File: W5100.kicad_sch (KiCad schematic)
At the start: 71 parts, among them J1 ARJM11C7-114-BA-EW2, T1 FA2805, U2 W5100, U3 TLV431DBZ, U4 VO615A, U5 SI3402, Y2 25MHz

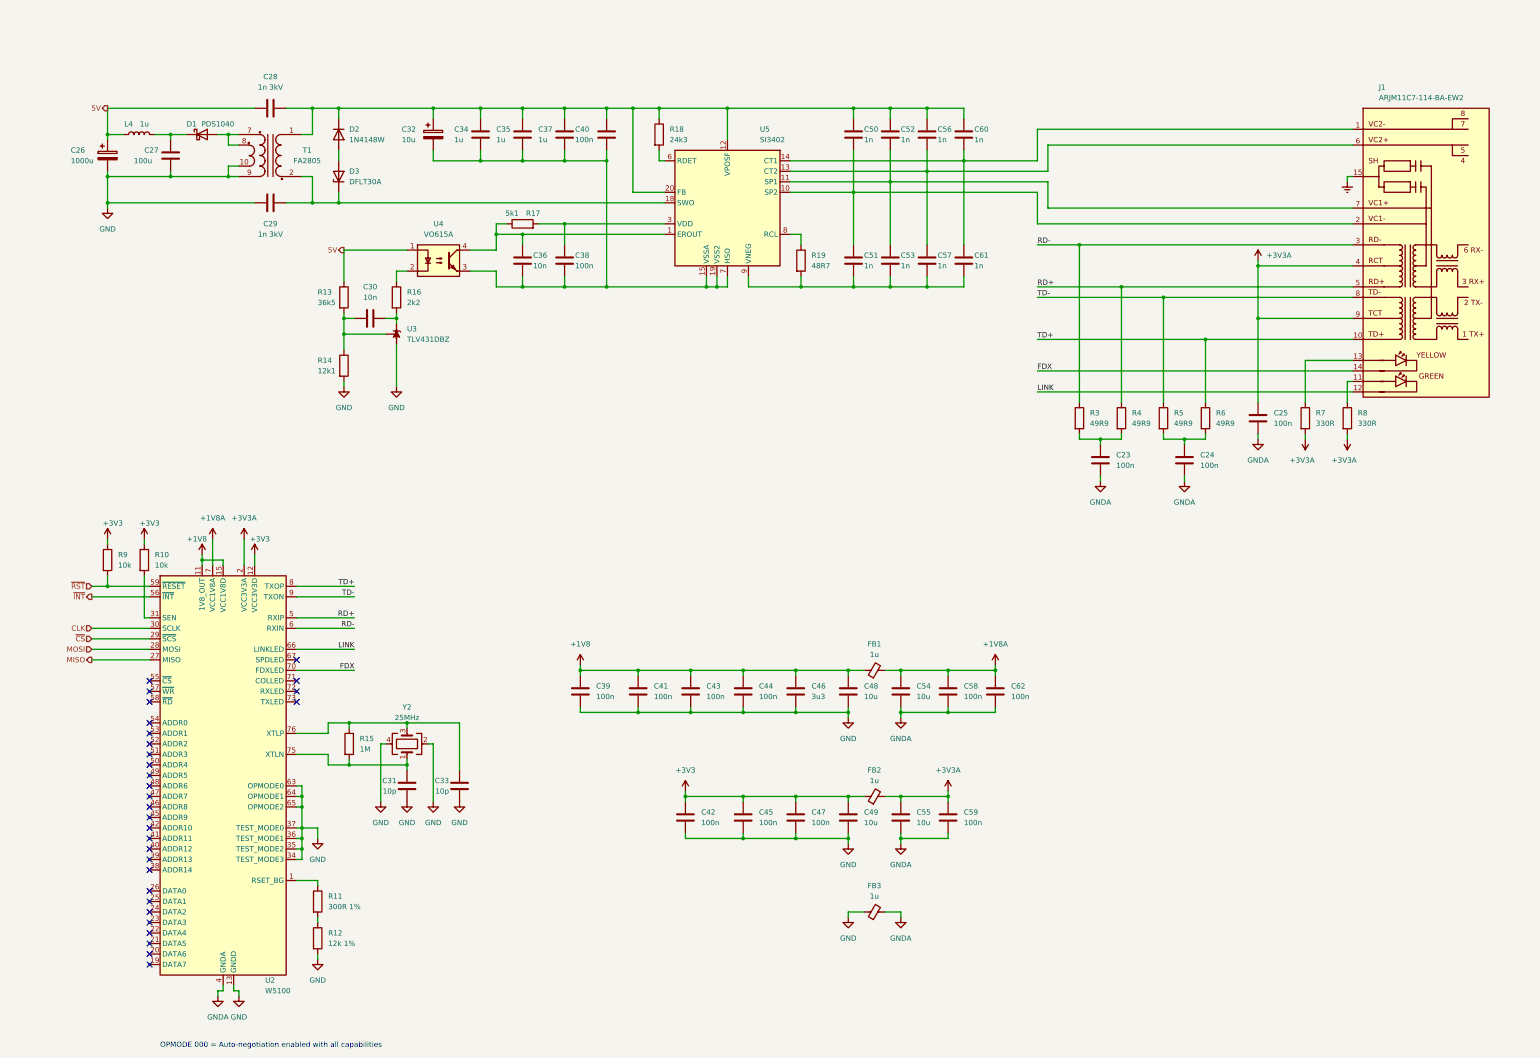
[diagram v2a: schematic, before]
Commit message: Added USB port
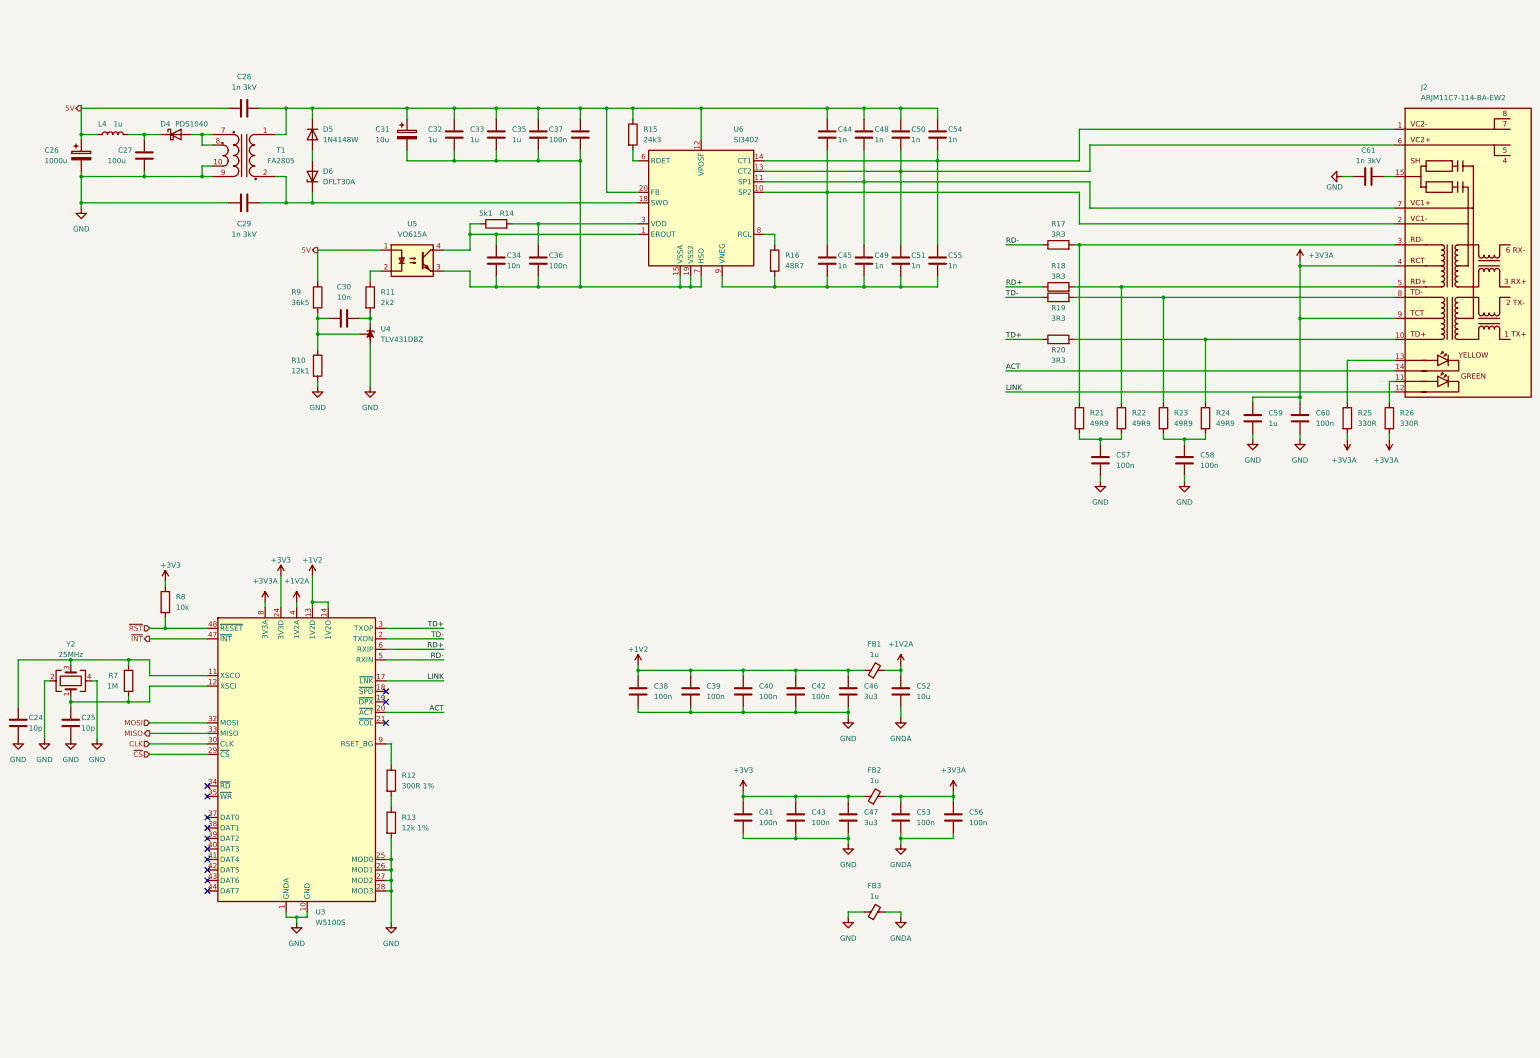
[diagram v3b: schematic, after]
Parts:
- removed C31, C33: 10p, symbol Device:C
- removed C42, C58, C62: 100n, symbol Device:C
- removed C48, C55: 10u, symbol Device:C
- removed R10, R9: 10k, symbol Device:R
- removed R11: 300R 1%, symbol Device:R
- removed R15: 1M, symbol Device:R
- removed U2: W5100, Package_QFP:LQFP-80_10x10mm_P0.4mm, symbol Interface_Ethernet:W5100
- added C24, C25: 10p, Capacitor_SMD:C_0402_1005Metric, symbol Device:C
- added C56: 100n, Capacitor_SMD:C_0402_1005Metric, symbol Device:C
- added C59: 1u, Capacitor_SMD:C_0402_1005Metric, symbol Device:C
- added C61: 1n 3kV, symbol Device:C
- added R13: 12k 1%, Resistor_SMD:R_0402_1005Metric, symbol Device:R
- added R17, R18, R19, R20: 3R3, Resistor_SMD:R_0402_1005Metric, symbol Device:R
- added R7: 1M, Resistor_SMD:R_0402_1005Metric, symbol Device:R
- added R8: 10k, Resistor_SMD:R_0402_1005Metric, symbol Device:R
- added U3: W5100S, Package_DFN_QFN:QFN-48-1EP_7x7mm_P0.5mm_EP5.3x5.3mm, symbol wiznet:W5100S
- C30, FB1, FB2, FB3, L4: footprint (none) -> Capacitor_SMD:C_0402_1005Metric
- C31: renamed from C32; footprint (none) -> Capacitor_SMD:C_0402_1005Metric
- C32: renamed from C34; footprint (none) -> Capacitor_SMD:C_0402_1005Metric
- C33: renamed from C35; footprint (none) -> Capacitor_SMD:C_0402_1005Metric
- C34: renamed from C36; footprint (none) -> Capacitor_SMD:C_0402_1005Metric
- C35: renamed from C37; footprint (none) -> Capacitor_SMD:C_0402_1005Metric
- C36: renamed from C38; footprint (none) -> Capacitor_SMD:C_0402_1005Metric
- C37: renamed from C40; footprint (none) -> Capacitor_SMD:C_0402_1005Metric
- C38: renamed from C39; footprint (none) -> Capacitor_SMD:C_0402_1005Metric
- C39: renamed from C41; footprint (none) -> Capacitor_SMD:C_0402_1005Metric
- C40: renamed from C43; footprint (none) -> Capacitor_SMD:C_0402_1005Metric
- C41: renamed from C45; footprint (none) -> Capacitor_SMD:C_0402_1005Metric
- C42: renamed from C44; footprint (none) -> Capacitor_SMD:C_0402_1005Metric
- C43: renamed from C47; footprint (none) -> Capacitor_SMD:C_0402_1005Metric
- C44: renamed from C50; footprint (none) -> Capacitor_SMD:C_0402_1005Metric
- C45: renamed from C51; footprint (none) -> Capacitor_SMD:C_0402_1005Metric
- C47: renamed from C49; value 10u -> 3u3
- C48: renamed from C52; footprint (none) -> Capacitor_SMD:C_0402_1005Metric
- C49: renamed from C53; footprint (none) -> Capacitor_SMD:C_0402_1005Metric
- C50: renamed from C56; footprint (none) -> Capacitor_SMD:C_0402_1005Metric
- C51: renamed from C57; footprint (none) -> Capacitor_SMD:C_0402_1005Metric
- C53: renamed from C59; footprint (none) -> Capacitor_SMD:C_0402_1005Metric
- C54: renamed from C60; footprint (none) -> Capacitor_SMD:C_0402_1005Metric
- C55: renamed from C61; footprint (none) -> Capacitor_SMD:C_0402_1005Metric
- C57: renamed from C23; footprint (none) -> Capacitor_SMD:C_0402_1005Metric
- C58: renamed from C24; footprint (none) -> Capacitor_SMD:C_0402_1005Metric
- C60: renamed from C25; footprint (none) -> Capacitor_SMD:C_0402_1005Metric
- R10: renamed from R14; footprint (none) -> Resistor_SMD:R_0402_1005Metric
- R11: renamed from R16; footprint (none) -> Resistor_SMD:R_0402_1005Metric
- R12: value 12k 1% -> 300R 1%; footprint (none) -> Resistor_SMD:R_0402_1005Metric
- R14: renamed from R17; footprint (none) -> Resistor_SMD:R_0402_1005Metric
- R15: renamed from R18; footprint (none) -> Resistor_SMD:R_0402_1005Metric
- R16: renamed from R19; footprint (none) -> Resistor_SMD:R_0402_1005Metric
- R21: renamed from R3; footprint (none) -> Resistor_SMD:R_0402_1005Metric
- R22: renamed from R4; footprint (none) -> Resistor_SMD:R_0402_1005Metric
- R23: renamed from R5; footprint (none) -> Resistor_SMD:R_0402_1005Metric
- R24: renamed from R6; footprint (none) -> Resistor_SMD:R_0402_1005Metric
- R25: renamed from R7; footprint (none) -> Resistor_SMD:R_0402_1005Metric
- R26: renamed from R8; footprint (none) -> Resistor_SMD:R_0402_1005Metric
- R9: renamed from R13; footprint (none) -> Resistor_SMD:R_0402_1005Metric
- T1: footprint (none) -> coilcraft:Transformer_Coilcraft_Si3402
- U6: renamed from U5; footprint (none) -> skyworks:Skyworks_QFN-20_1EP5x5mm_P0.8mm_EP2.7x2.7mm
- renumbered C54 to C52, D1 to D4, D2 to D5, D3 to D6, J1 to J2, U3 to U4, U4 to U5
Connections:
- net +3V3: now also R8.1, U3.24 (3V3D), U3.36 (3V3D)
- net +3V3A: now also C56.1, C59.1, U3.15 (3V3A), U3.8 (3V3A)
- net CLK: now also U3.30 (CLK)
- net GND: now also C57.2, C58.2, C60.2, C24.2, C25.2, C59.2, C61.1, R13.2, U3.1 (GNDA), U3.10 (GND), U3.16 (GNDA), U3.23 (GND), U3.25 (MOD0), U3.26 (MOD1), U3.27 (MOD2), U3.28 (MOD3), U3.46 (GND), U3.7 (GNDA); no longer R12.2
- net GNDA: now also C56.2; no longer C57.2, C58.2, C60.2
- net LINK: now also U3.17 (~{LNK})
- net MISO: now also U3.33 (MISO)
- net MOSI: now also U3.32 (MOSI)
- net RD+: now also R18.1, U3.6 (RXIP); no longer J2.5, R22.1
- net RD-: now also R17.1, U3.5 (RXIN); no longer J2.3, R21.1
- net TD+: now also R20.1, U3.3 (TXOP); no longer J2.10, R24.1
- net TD-: now also R19.1, U3.2 (TXON); no longer J2.8, R23.1
- net ~{CS}: now also U3.29 (~{CS})
- net ~{INT}: now also U3.47 (~{INT})
- net ~{RST}: now also R8.2, U3.48 (~{RESET})
- net at Y2.3: now also C24.1, R7.1, U3.11 (XSCO)
- net at R12.1: now also U3.9 (RSET_BG)
- net at Y2.1: now also C25.1, R7.2, U3.12 (XSCI)
- net +1V8 renamed +1V2
- net +1V2: now also U3.13 (1V2D), U3.14 (1V2O), U3.22 (1V2D), U3.31 (1V2D), U3.45 (1V2D)
- net +1V8A renamed +1V2A
- net +1V2A: now also U3.4 (1V2A)
- net Earth: no longer names the net of J2.15
- net Earth: now also C61.2
- net FDX renamed ACT
- net ACT: now also U3.20 (~{ACT})
- new net: R12.2, R13.1
- new net: J2.8, R19.2, R23.1
- new net: J2.10, R20.2, R24.1
- new net: J2.3, R17.2, R21.1
- new net: J2.5, R18.2, R22.1
- no-connect marks 30 -> 13
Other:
- note removed: "OPMODE 000 = Auto-negotiation enabled with all capabilities"
- moved on the sheet: C26, C27, C28, C29, C30, C31, C32, C33, C34, C35, C36, C37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
